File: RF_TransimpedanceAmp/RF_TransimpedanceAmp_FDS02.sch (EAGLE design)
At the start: 39 parts, among them IC1 LT1964-5, IC2 OPA847, IC3 PMA-5452, IC4 ADM7150ARDZ-3.0, IC5 ADM7150ARDZ-5.0, IC6 PMA-5452

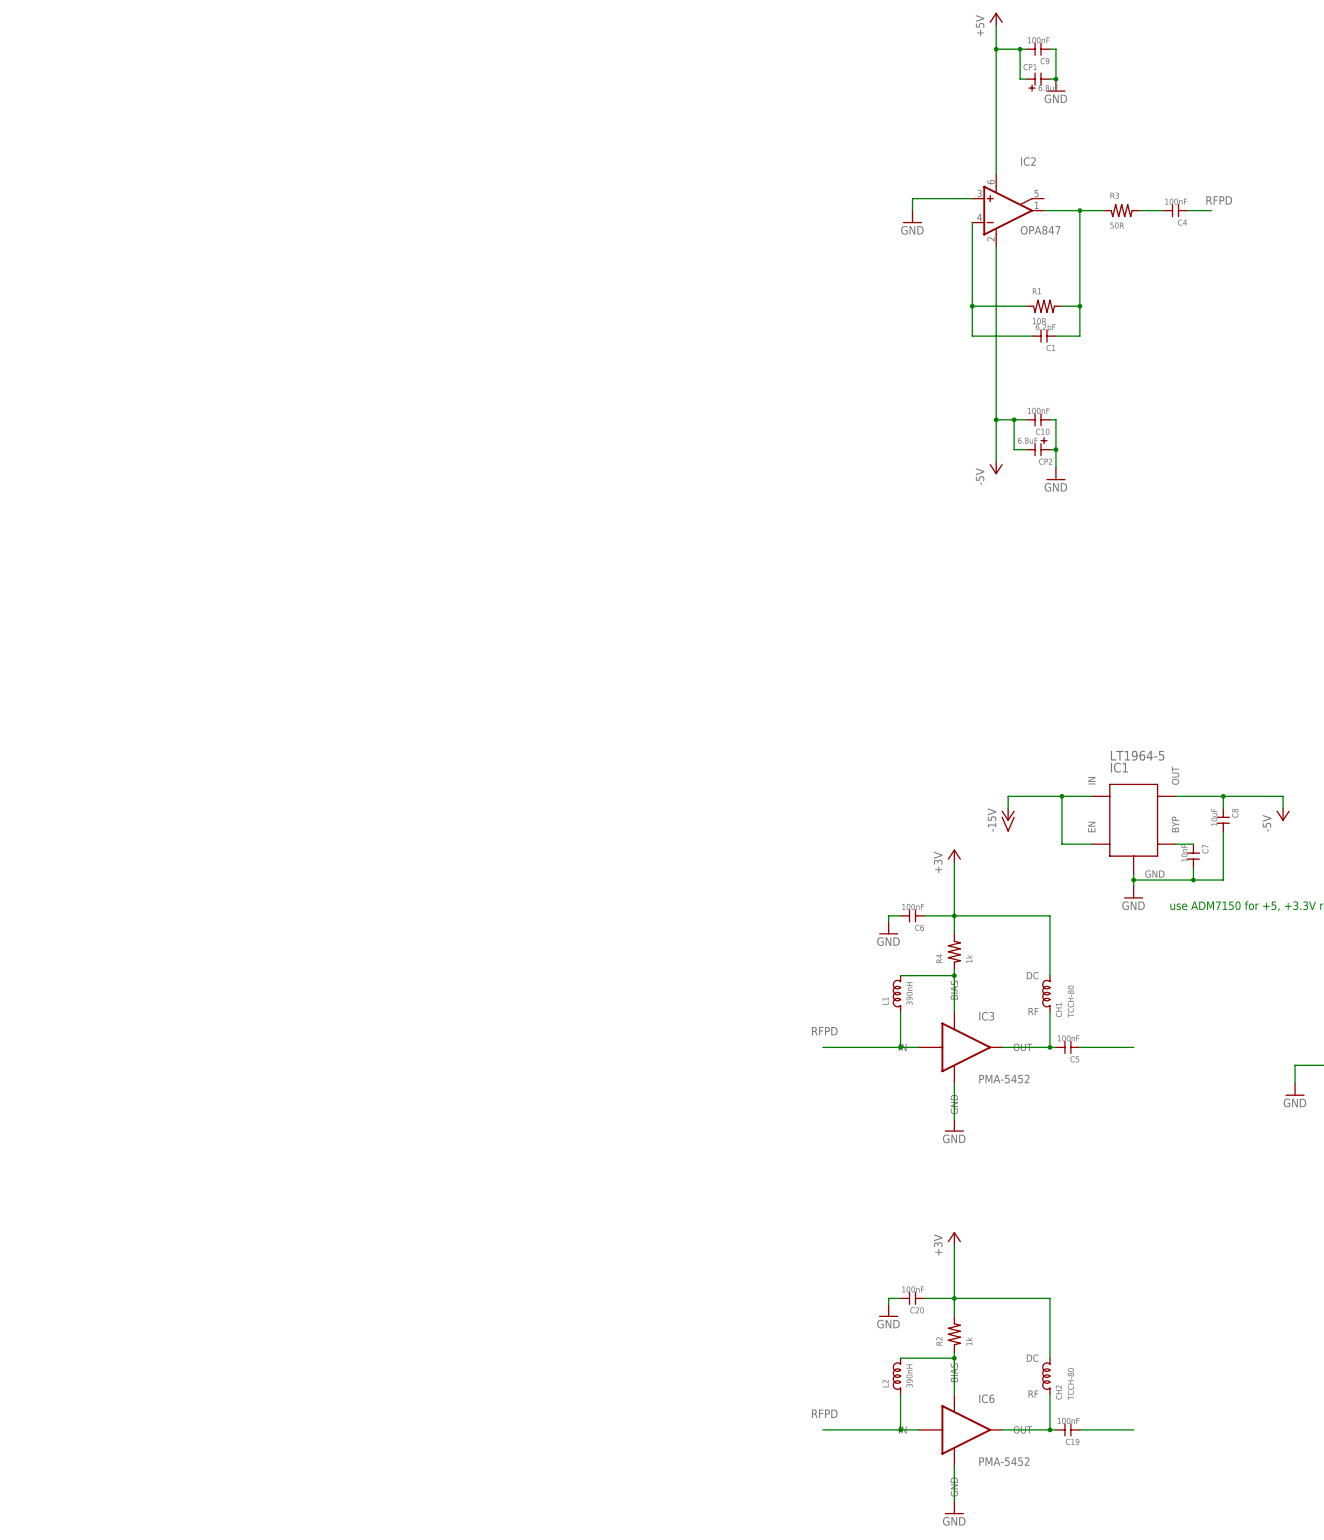
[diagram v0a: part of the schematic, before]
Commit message: First draft schematic and layout for FDS02 transimpedance amplifier.
* Low transimpedance gain, followed by low-noise RF amplifier.
* FDS02 is FC-connectorized, mount on bottom of board and standoff from front panel.

TODO:
* Remove -5V supply?
* Compare OPA847 vs some FET-input op amp
* Filtering on PD bias voltage?
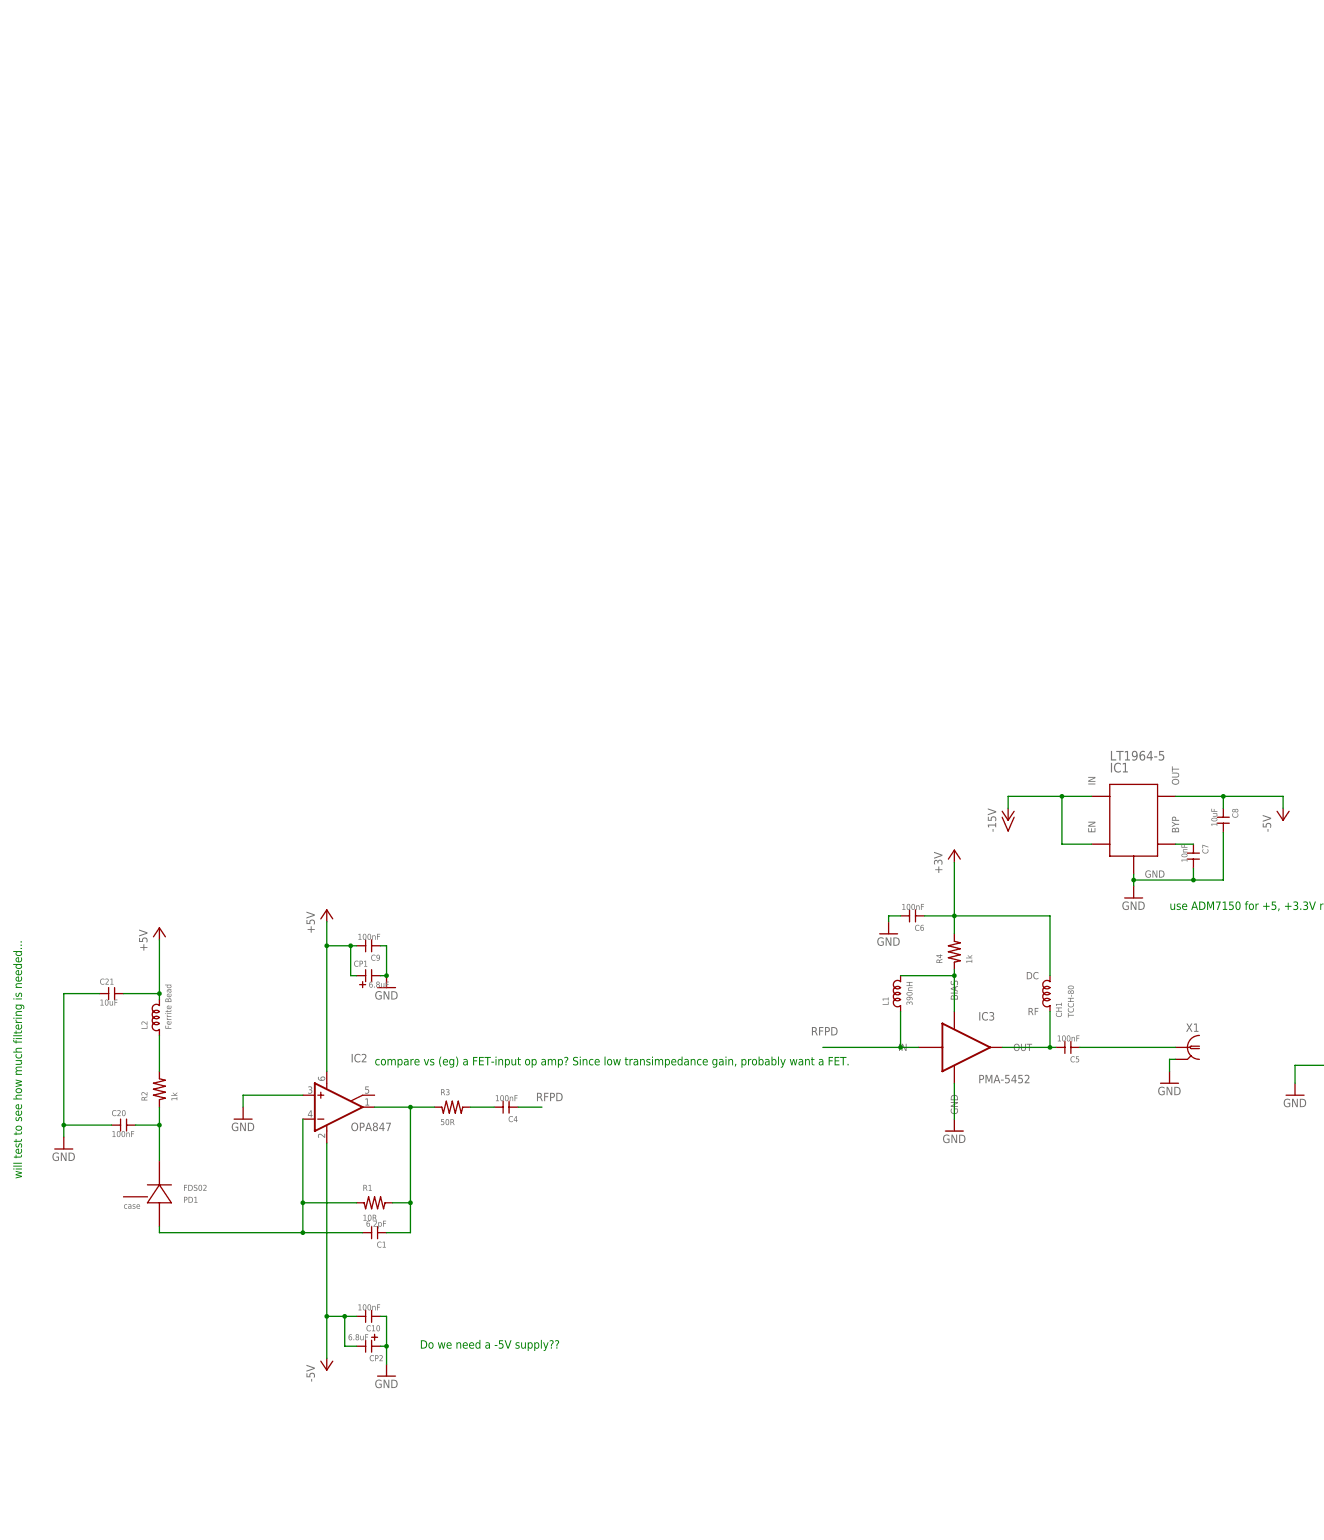
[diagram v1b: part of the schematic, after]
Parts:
- removed C19: 100nF, rlc-jqi:CAP0402
- removed CH2: TCCH-80, rf-jqi:TCCH-80
- removed IC6: PMA-5452, rf-jqi:PMA-5452
- added C21: 10uF, rlc-jqi:CAP1210
- added PD1: FDS02, semiconductor-jqi:FDS02
- added X1: SMAJ502, connector-jqi:SMAJ502
- L2: value 390nH -> Ferrite Bead; device rlc-jqi:INDUCTOR-0402 -> rlc-jqi:INDUCTOR-1206; PARTNO (none) -> 445-5223-1-ND
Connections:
- removed net N$11: IC6.BIAS, L2.P$2, R2.P$1
- net +3V: no longer C20.P$1, CH2.DC, R2.P$2
- net +5V: now also C21.P$2, L2.P$2
- net GND: now also C20.P$1, C21.P$1, X1.2; no longer C20.P$2, IC6.GND
- net N$2: now also PD1.ANODE
- net N$5: now also L2.P$1, R2.P$2; no longer C19.P$2, CH2.RF, IC6.OUT
- net N$7: now also X1.1
- net N$8: now also C20.P$2, PD1.CATHODE, R2.P$1; no longer C19.P$1
- net RFPD: no longer IC6.IN, L2.P$1
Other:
- note added: "Do we need a -5V supply??"
- note added: "compare vs (eg) a FET-input op amp? Since low transimpedance gain, probably want a FET."
- note added: "will test to see how much filtering is needed..."
- moved on the sheet: C1, C10, C20, C4, C9, CP1, CP2, IC2, L2, R1, R2, R3

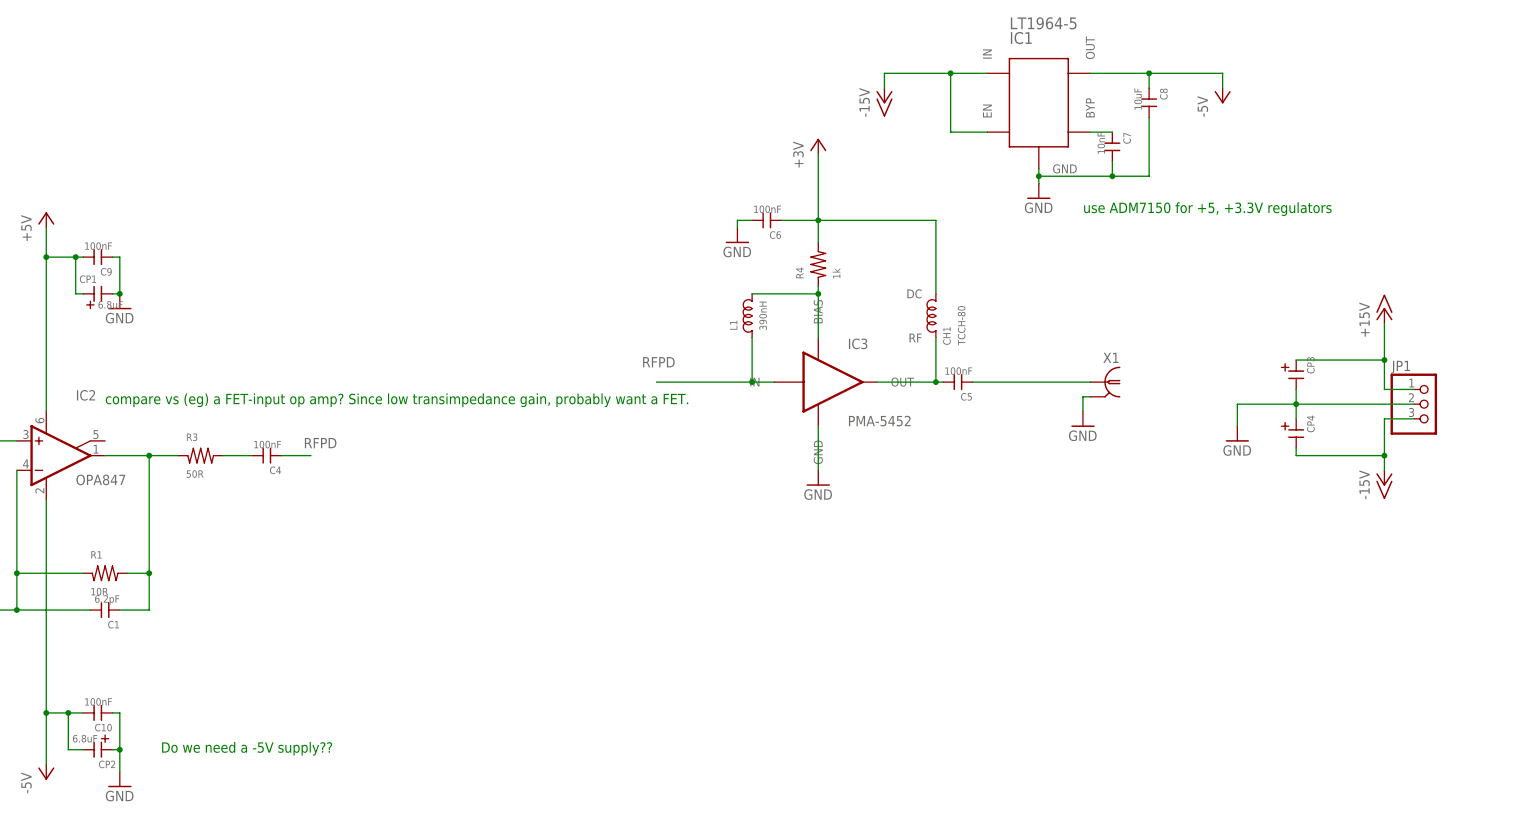
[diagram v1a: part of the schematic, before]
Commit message: Minor tweaks to schematic notes; need to check 50 ohm trace width then ready to print.
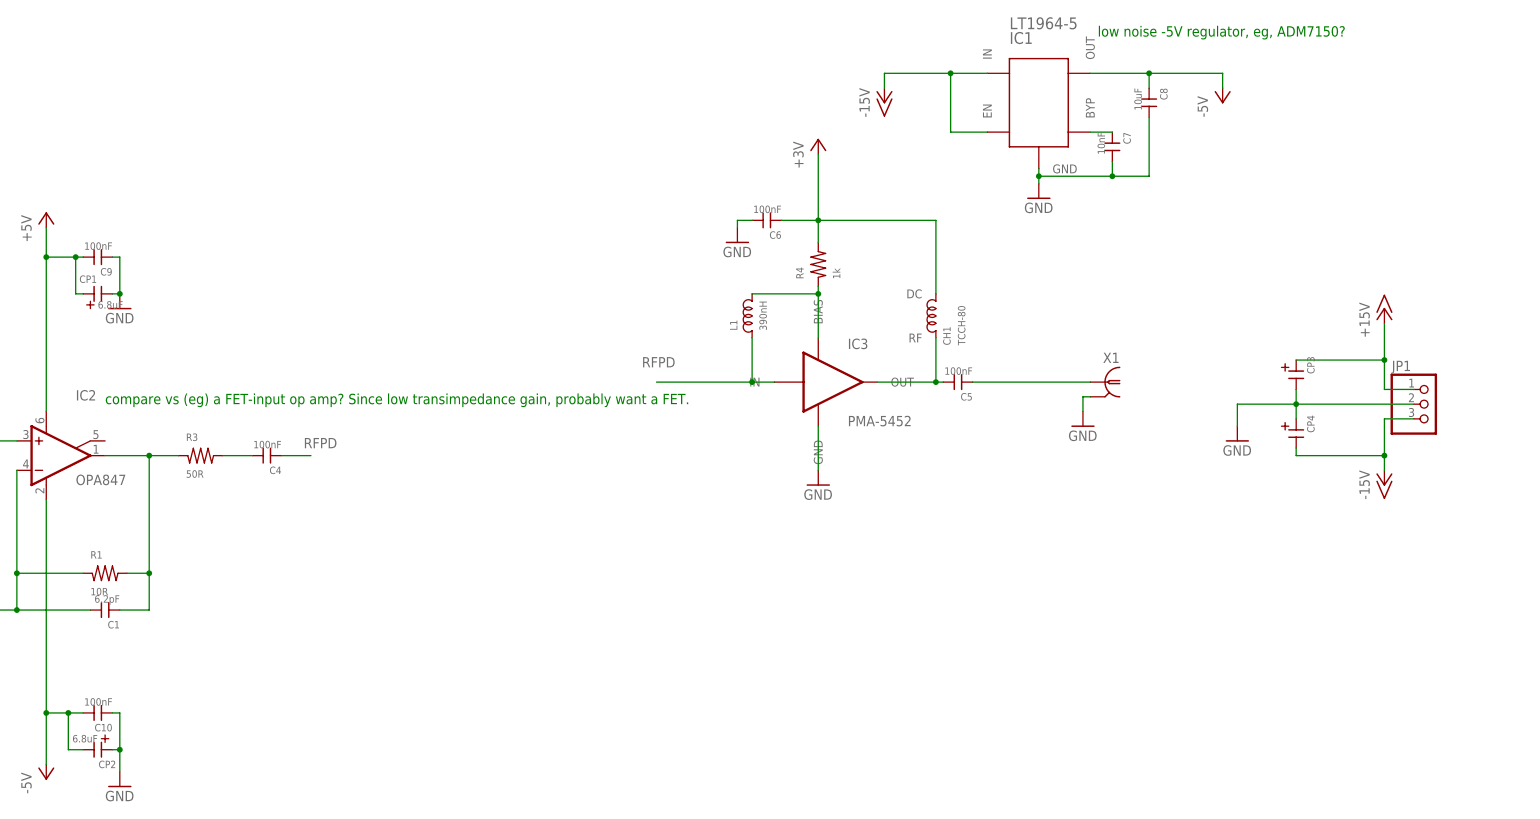
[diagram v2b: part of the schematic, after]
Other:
- note added: "low noise -5V regulator, eg, ADM7150?"
- note removed: "Do we need a -5V supply??"
- note removed: "use ADM7150 for +5, +3.3V regulators"
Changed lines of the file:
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@@
 <setting verticaltext="up"/>
 </settings>
-<grid distance="0.05" unitdist="inch" unit="inch" style="lines" multiple="1" display="no" altdistance="0.01" altunitdist="inch" altunit="inch"/>
+<grid distance="0.1" unitdist="inch" unit="inch" style="lines" multiple="1" display="no" altdistance="0.01" altunitdist="inch" altunit="inch"/>
 <layers>
 <layer number="1" name="Top" color="4" fill="1" visible="no" active="no"/>
@@
 <sheet>
 <plain>
-<text x="96.52" y="73.66" size="1.778" layer="91">use ADM7150 for +5, +3.3V regulators</text>
 <text x="-147.32" y="16.51" size="1.778" layer="91" rot="R90">will test to see how much filtering is needed...</text>
-<text x="-33.02" y="-17.78" size="1.778" layer="91" rot="R180">Do we need a -5V supply??</text>
 <text x="-72.39" y="40.64" size="1.778" layer="91">compare vs (eg) a FET-input op amp? Since low transimpedance gain, probably want a FET.</text>
+<text x="99.06" y="104.14" size="1.778" layer="91">low noise -5V regulator, eg, ADM7150?</text>
 </plain>
 <instances>

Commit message: Removed OPA847, using low-noise amplifiers with 50 ohm input as transimpedance gain.
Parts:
- removed C10, C9: 100nF, rlc-jqi:CAP0402
- removed C21, C8: 10uF, rlc-jqi:CAP1210
- removed C7: 10nF, rlc-jqi:CAP0402
- removed CP1, CP2: 6.8uF, rlc-jqi:CAP-POL0603
- removed CP4: (no value), rlc-jqi:CAP-POLPANASONIC_F
- removed IC2: OPA847, opamp-jqi:OPAMP-6PIN-SOT23-6
- removed R3: 50R, rlc-jqi:RES0402
- added CH2: TCCH-80, rf-jqi:TCCH-80
- added L3: 390nH, rlc-jqi:INDUCTOR-0402
- C1: value 6.2pF -> 100nF
- IC1: value LT1964-5 -> PMA-5452; device regulator-jqi:LT1964-5 -> rf-jqi:PMA-5452
- JP1: device pinhead:PINHD-1X3 -> pinhead:PINHD-1X2
- R1: value 10R -> 1k
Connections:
- removed net -15V: CP4.P$2, IC1.EN, IC1.IN, JP1.3
- removed net -5V: C10.P$2, C8.P$1, CP2.P$2, IC1.OUT, IC2.V-
- removed net N$10: C7.P$1, IC1.BYP
- removed net N$4: C4.P$2, R3.P$2
- removed net N$5 (its old number): L2.P$1, R2.P$2
- new net RFPD1: C4.P$1, IC1.IN, L3.P$1
- net +3V: now also C1.P$1, CH2.DC, R1.P$2
- net +5V: now also R2.P$2; no longer C21.P$2, C9.P$2, CP1.P$1, IC2.V+, L2.P$2
- net GND: now also C1.P$2, L2.P$1; no longer C10.P$1, C21.P$1, C7.P$2, C8.P$2, C9.P$1, CP1.P$2, CP2.P$1, CP4.P$1, IC2.+IN
- net N$2: now also C5.P$2, CH2.RF, IC1.OUT; no longer C1.P$2, IC2.-IN, PD1.ANODE, R1.P$1
- net N$3: now also IC1.BIAS, L3.P$2, R1.P$1; no longer C1.P$1, IC2.OUT, R1.P$2, R3.P$1
- net N$6: now also C4.P$2; no longer C5.P$2
- net RFPD: now also L2.P$2, PD1.ANODE; no longer C4.P$1
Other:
- note removed: "compare vs (eg) a FET-input op amp? Since low transimpedance gain, probably want a FET."
- note removed: "low noise -5V regulator, eg, ADM7150?"
- note removed: "will test to see how much filtering is needed..."
- moved on the sheet: C1, C11, C12, C13, C14, C15, C16, C17, C18, C2, C20, C3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
